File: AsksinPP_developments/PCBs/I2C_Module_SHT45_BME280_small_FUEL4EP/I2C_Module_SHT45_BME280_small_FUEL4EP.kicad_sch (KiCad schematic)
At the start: 13 parts, among them J1 Conn_01x04, U1 BME280, U2 SHT45-AD1B-R2

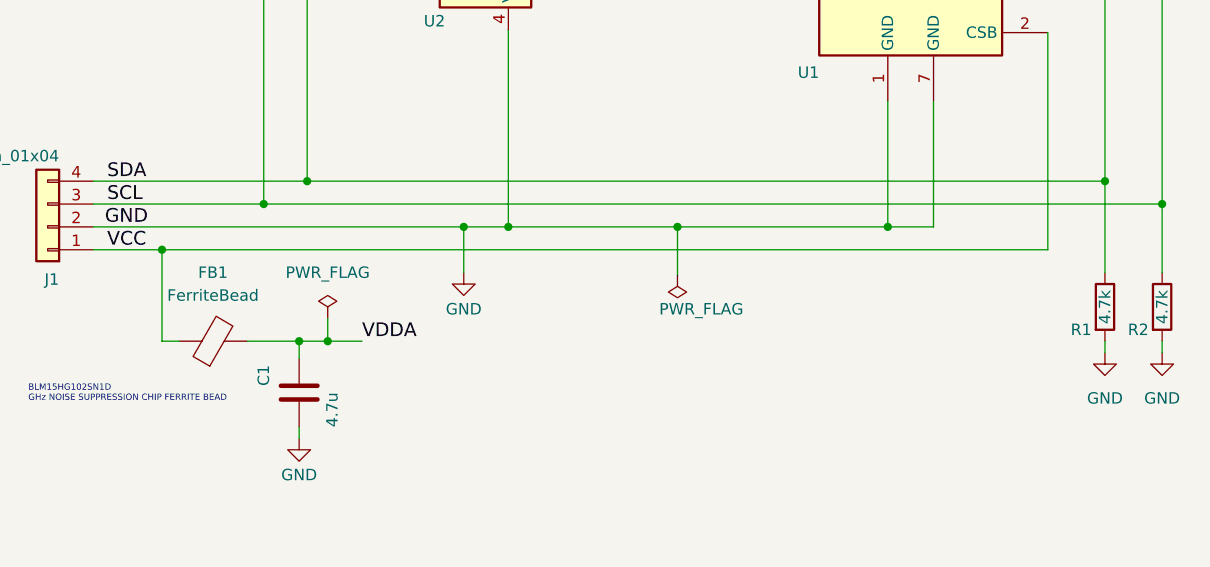
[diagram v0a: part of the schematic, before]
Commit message: PCBs: fix of some project specific KiCAD library paths for portability and missing PWR_FLGs for VCC in some schematics
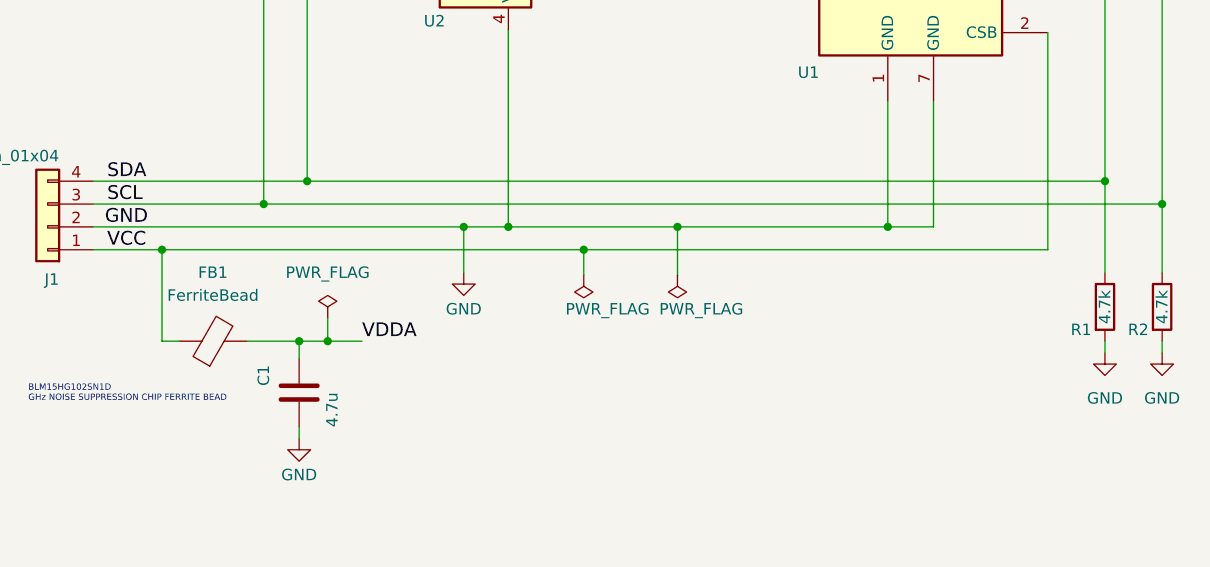
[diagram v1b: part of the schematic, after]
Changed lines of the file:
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@@
   (title_block
     (title "I2C_Module_SHT45_BME280_small_FUEL4EP")
-    (date "2024-01-13")
-    (rev "1.0")
+    (date "2024-01-14")
+    (rev "1.1")
     (company "FUEL4EP")
     (comment 1 "fitting to  HB_Stamp_ATMega1284P_FUEL4EP")
@@
   (junction (at 82.55 124.46) (diameter 0) (color 0 0 0 0)
   )
+  (junction (at 110.998 114.3) (diameter 0) (color 0 0 0 0)
+  )
   (junction (at 102.616 111.76) (diameter 0) (color 0 0 0 0)
   )
@@
     (stroke (width 0) (type default) (color 0 0 0 0))
   )
+  (wire (pts (xy 110.998 114.3) (xy 162.56 114.3))
+    (stroke (width 0) (type default) (color 0 0 0 0))
+  )
   (wire (pts (xy 121.412 111.76) (xy 144.78 111.76))
     (stroke (width 0) (type default) (color 0 0 0 0))
@@
     (stroke (width 0) (type default) (color 0 0 0 0))
   )
+  (wire (pts (xy 110.998 117.094) (xy 110.998 114.3))
+    (stroke (width 0) (type default) (color 0 0 0 0))
+  )
   (wire (pts (xy 79.375 133.985) (xy 79.375 135.255))
     (stroke (width 0) (type default) (color 0 0 0 0))
@@
     (stroke (width 0) (type default) (color 0 0 0 0))
   )
-  (wire (pts (xy 64.135 114.3) (xy 162.56 114.3))
+  (wire (pts (xy 64.135 114.3) (xy 110.998 114.3))
     (stroke (width 0) (type default) (color 0 0 0 0))
   )
@@
     (pin "8")
   )
+  (symbol (lib_id "power:PWR_FLAG") (at 110.998 117.094 180) (unit 1)
+    (in_bom yes) (on_board yes)
+    (property "Reference" "#FLG0102" (id 0) (at 110.998 118.999 0)
+      (effects (font (size 1.27 1.27)) hide)
+    )
+    (property "Value" "PWR_FLAG" (id 1) (at 108.966 120.904 0)
+      (effects (font (size 1.27 1.27)) (justify right))
+    )
+    (property "Footprint" "" (id 2) (at 110.998 117.094 0)
+      (effects (font (size 1.27 1.27)) hide)
+    )
+    (property "Datasheet" "~" (id 3) (at 110.998 117.094 0)
+      (effects (font (size 1.27 1.27)) hide)
+    )
+    (pin "1")
+  )
   (symbol (lib_id "Device:C") (at 79.375 130.175 0) (unit 1)
     (in_bom yes) (on_board yes)
@@
       (reference "#FLG0101") (unit 1) (value "PWR_FLAG") (footprint "")
     )
+    (path "/7820c09a-77a5-4506-a798-0f22336e0c44"
+      (reference "#FLG0102") (unit 1) (value "PWR_FLAG") (footprint "")
+    )
     (path "/2fb280af-9352-43f7-93d8-89326fb5dc6f"

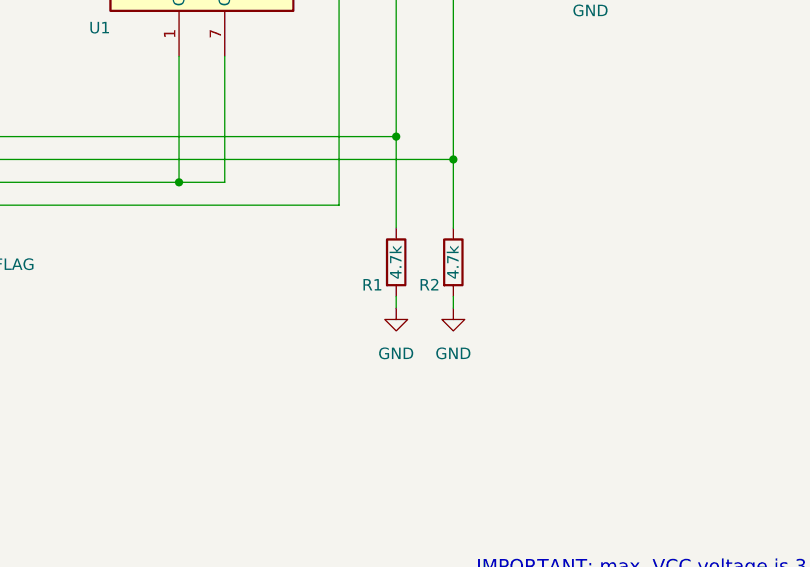
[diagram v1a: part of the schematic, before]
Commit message: PCBs: fix of I2C Pull-up resistors that were wrongly tied to GND
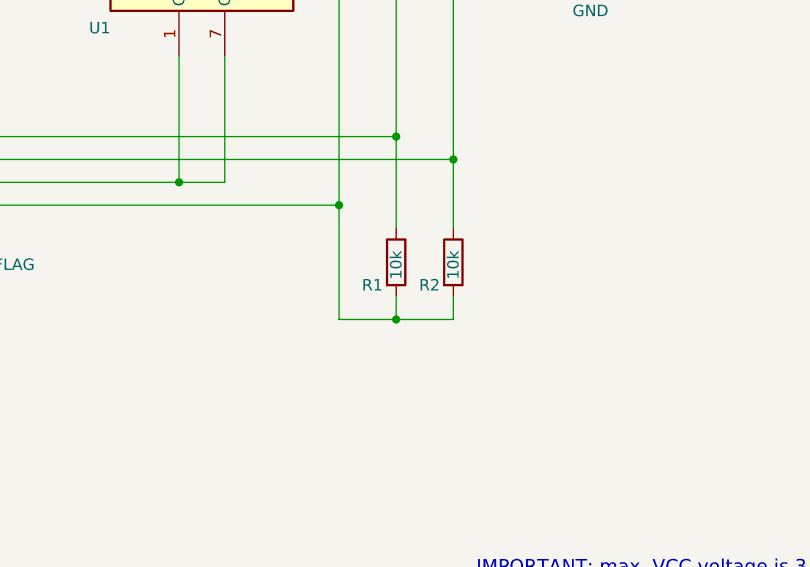
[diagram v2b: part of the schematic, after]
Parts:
- R1, R2: value 4.7k -> 10k; LCSC C25900 -> C25744
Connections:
- net GND: no longer R1.2, R2.2
- net VCC: now also R1.2, R2.2
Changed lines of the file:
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@@
   (title_block
     (title "I2C_Module_SHT45_BME280_small_FUEL4EP")
-    (date "2024-01-14")
-    (rev "1.1")
+    (date "2024-02-08")
+    (rev "1.2")
     (company "FUEL4EP")
     (comment 1 "fitting to  HB_Stamp_ATMega1284P_FUEL4EP")
@@
   (junction (at 64.135 114.3) (diameter 0) (color 0 0 0 0)
   )
+  (junction (at 162.56 114.3) (diameter 0) (color 0 0 0 0)
+  )
   (junction (at 154.94 58.42) (diameter 0) (color 0 0 0 0)
   )
+  (junction (at 168.91 127) (diameter 0) (color 0 0 0 0)
+  )
   (junction (at 79.375 124.46) (diameter 0) (color 0 0 0 0)
   )
@@
     (stroke (width 0) (type default) (color 0 0 0 0))
   )
+  (wire (pts (xy 162.56 127) (xy 162.56 114.3))
+    (stroke (width 0) (type default) (color 0 0 0 0))
+  )
   (wire (pts (xy 80.264 106.68) (xy 168.91 106.68))
     (stroke (width 0) (type default) (color 0 0 0 0))
@@
     (stroke (width 0) (type default) (color 0 0 0 0))
   )
-  (wire (pts (xy 168.91 124.46) (xy 168.91 125.73))
-    (stroke (width 0) (type default) (color 0 0 0 0))
-  )
   (wire (pts (xy 56.515 106.68) (xy 80.264 106.68))
     (stroke (width 0) (type default) (color 0 0 0 0))
@@
     (stroke (width 0) (type default) (color 0 0 0 0))
   )
-  (wire (pts (xy 175.26 124.46) (xy 175.26 125.73))
-    (stroke (width 0) (type default) (color 0 0 0 0))
-  )
   (wire (pts (xy 149.86 58.42) (xy 154.94 58.42))
     (stroke (width 0) (type default) (color 0 0 0 0))
@@
     (stroke (width 0) (type default) (color 0 0 0 0))
   )
+  (wire (pts (xy 168.91 127) (xy 162.56 127))
+    (stroke (width 0) (type default) (color 0 0 0 0))
+  )
+  (wire (pts (xy 175.26 124.46) (xy 175.26 127))
+    (stroke (width 0) (type default) (color 0 0 0 0))
+  )
   (wire (pts (xy 138.43 58.42) (xy 144.78 58.42))
     (stroke (width 0) (type default) (color 0 0 0 0))
@@
     (stroke (width 0) (type default) (color 0 0 0 0))
   )
+  (wire (pts (xy 175.26 127) (xy 168.91 127))
+    (stroke (width 0) (type default) (color 0 0 0 0))
+  )
   (wire (pts (xy 73.66 124.46) (xy 79.375 124.46))
     (stroke (width 0) (type default) (color 0 0 0 0))
@@
   )
   (wire (pts (xy 144.78 97.79) (xy 144.78 111.76))
+    (stroke (width 0) (type default) (color 0 0 0 0))
+  )
+  (wire (pts (xy 168.91 124.46) (xy 168.91 127))
     (stroke (width 0) (type default) (color 0 0 0 0))
   )
@@
       (effects (font (size 1.27 1.27)) (justify left))
     )
-    (property "Value" "4.7k" (id 1) (at 168.91 122.555 90)
+    (property "Value" "10k" (id 1) (at 168.91 122.555 90)
       (effects (font (size 1.27 1.27)) (justify left))
     )
@@
       (effects (font (size 1.27 1.27)) hide)
     )
-    (property "LCSC" "C25900" (id 4) (at 168.91 120.65 0)
+    (property "LCSC" "C25744" (id 4) (at 168.91 120.65 0)
       (effects (font (size 1.524 1.524)) hide)
     )
@@
     )
     (property "Datasheet" "" (id 3) (at 93.472 48.768 0)
-      (effects (font (size 1.27 1.27)) hide)
-    )
-    (pin "1")
-  )
-  (symbol (lib_id "power:GND") (at 168.91 125.73 0) (unit 1)
-    (in_bom yes) (on_board yes) (fields_autoplaced)
-    (property "Reference" "#PWR07" (id 0) (at 168.91 132.08 0)
-      (effects (font (size 1.27 1.27)) hide)
-    )
-    (property "Value" "GND" (id 1) (at 168.91 130.81 0))
-    (property "Footprint" "" (id 2) (at 168.91 125.73 0)
-      (effects (font (size 1.27 1.27)) hide)
-    )
-    (property "Datasheet" "" (id 3) (at 168.91 125.73 0)
       (effects (font (size 1.27 1.27)) hide)
     )
@@
     (pin "1")
   )
-  (symbol (lib_id "power:GND") (at 175.26 125.73 0) (unit 1)
-    (in_bom yes) (on_board yes) (fields_autoplaced)
-    (property "Reference" "#PWR08" (id 0) (at 175.26 132.08 0)
-      (effects (font (size 1.27 1.27)) hide)
-    )
-    (property "Value" "GND" (id 1) (at 175.26 130.81 0))
-    (property "Footprint" "" (id 2) (at 175.26 125.73 0)
-      (effects (font (size 1.27 1.27)) hide)
-    )
-    (property "Datasheet" "" (id 3) (at 175.26 125.73 0)
-      (effects (font (size 1.27 1.27)) hide)
-    )
-    (pin "1")
-  )
   (symbol (lib_id "power:VDDA") (at 167.64 48.26 0) (unit 1)
     (in_bom yes) (on_board yes) (fields_autoplaced)
@@
       (effects (font (size 1.27 1.27)) (justify left))
     )
-    (property "Value" "4.7k" (id 1) (at 175.26 122.555 90)
+    (property "Value" "10k" (id 1) (at 175.26 122.555 90)
       (effects (font (size 1.27 1.27)) (justify left))
     )
@@
       (effects (font (size 1.27 1.27)) hide)
     )
-    (property "LCSC" "C25900" (id 4) (at 175.26 120.65 0)
+    (property "LCSC" "C25744" (id 4) (at 175.26 120.65 0)
       (effects (font (size 1.524 1.524)) hide)
     )
@@
       (reference "#PWR06") (unit 1) (value "VDDA") (footprint "")
     )
-    (path "/18542ab6-239f-4332-a70c-3c8551b285bb"
-      (reference "#PWR07") (unit 1) (value "GND") (footprint "")
-    )
-    (path "/d43541cc-8fb7-4c57-a7c8-5b5588c55acf"
-      (reference "#PWR08") (unit 1) (value "GND") (footprint "")
-    )
     (path "/b9ee5250-0210-4fd4-abf8-6419214a066d"
       (reference "#PWR09") (unit 1) (value "GND") (footprint "")
@@
     )
     (path "/010452d5-e5f2-447e-a153-71da0dbec114"
-      (reference "R1") (unit 1) (value "4.7k") (footprint "Resistor_SMD:R_0402_1005Metric")
+      (reference "R1") (unit 1) (value "10k") (footprint "Resistor_SMD:R_0402_1005Metric")
     )
     (path "/f75dc7be-70bf-4119-8c06-195e1a960dd2"
-      (reference "R2") (unit 1) (value "4.7k") (footprint "Resistor_SMD:R_0402_1005Metric")
+      (reference "R2") (unit 1) (value "10k") (footprint "Resistor_SMD:R_0402_1005Metric")
     )
     (path "/55b96afd-ec19-4400-9134-cc56302d872a"

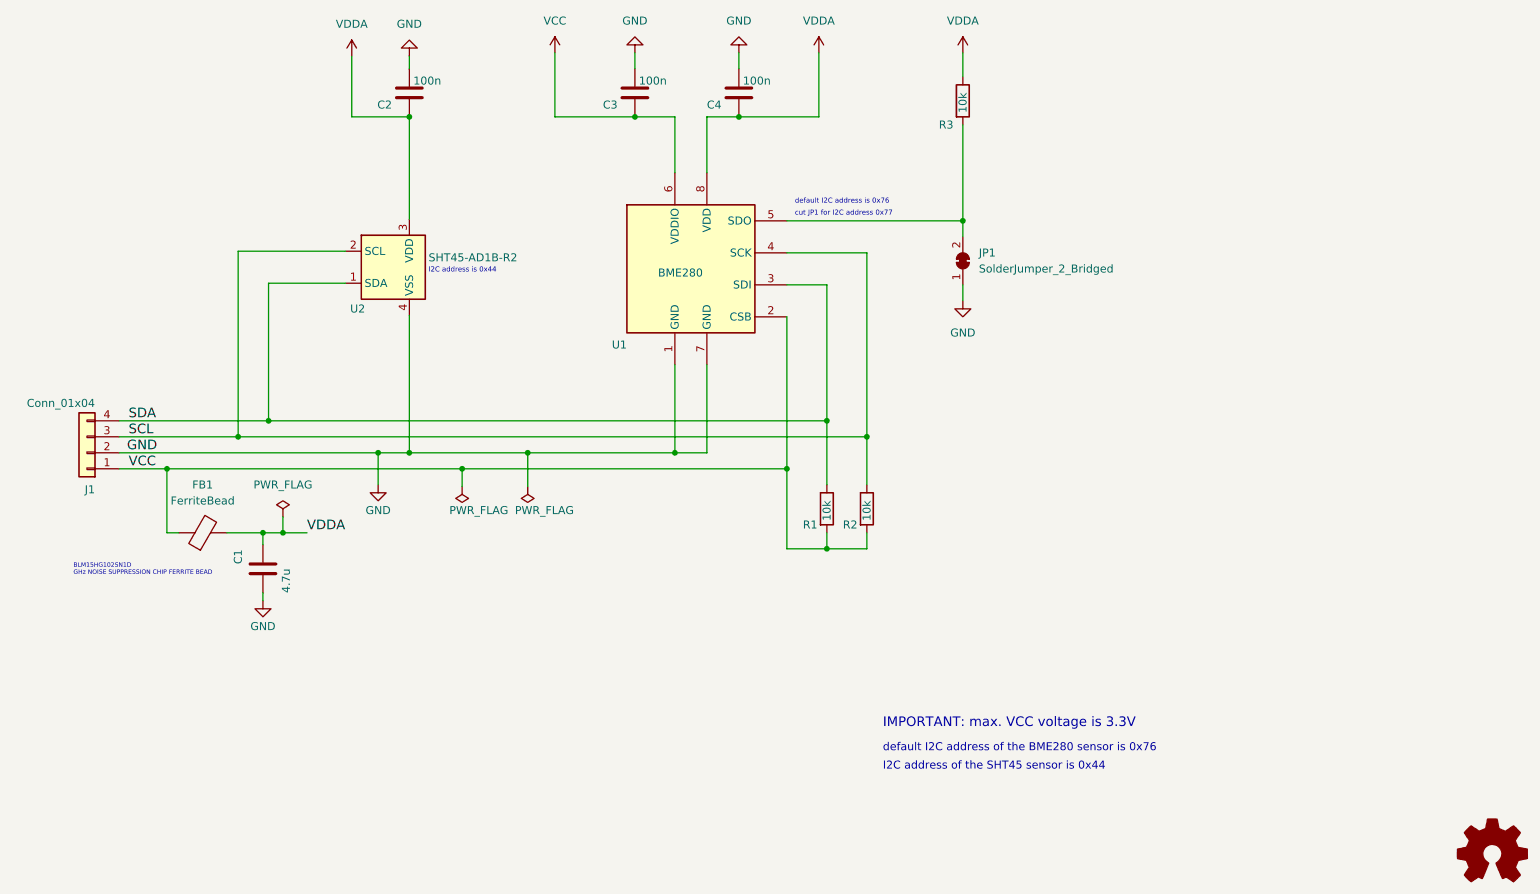
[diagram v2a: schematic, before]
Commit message: PCBs: upgrade some PCBs to KiCAD 7; fix of unnecessary leakage current of I2C address selector: I2C_Module_SHT85_BME280_FUEL4EP, I2C_Module_SHT45_BME280_small_FUEL4EP, I2C_Module_SHT45_BME280_FUEL4EP, I2C_Module_BME280_FUEL4EP, and I2C_Module_BME680_FUEL4EP
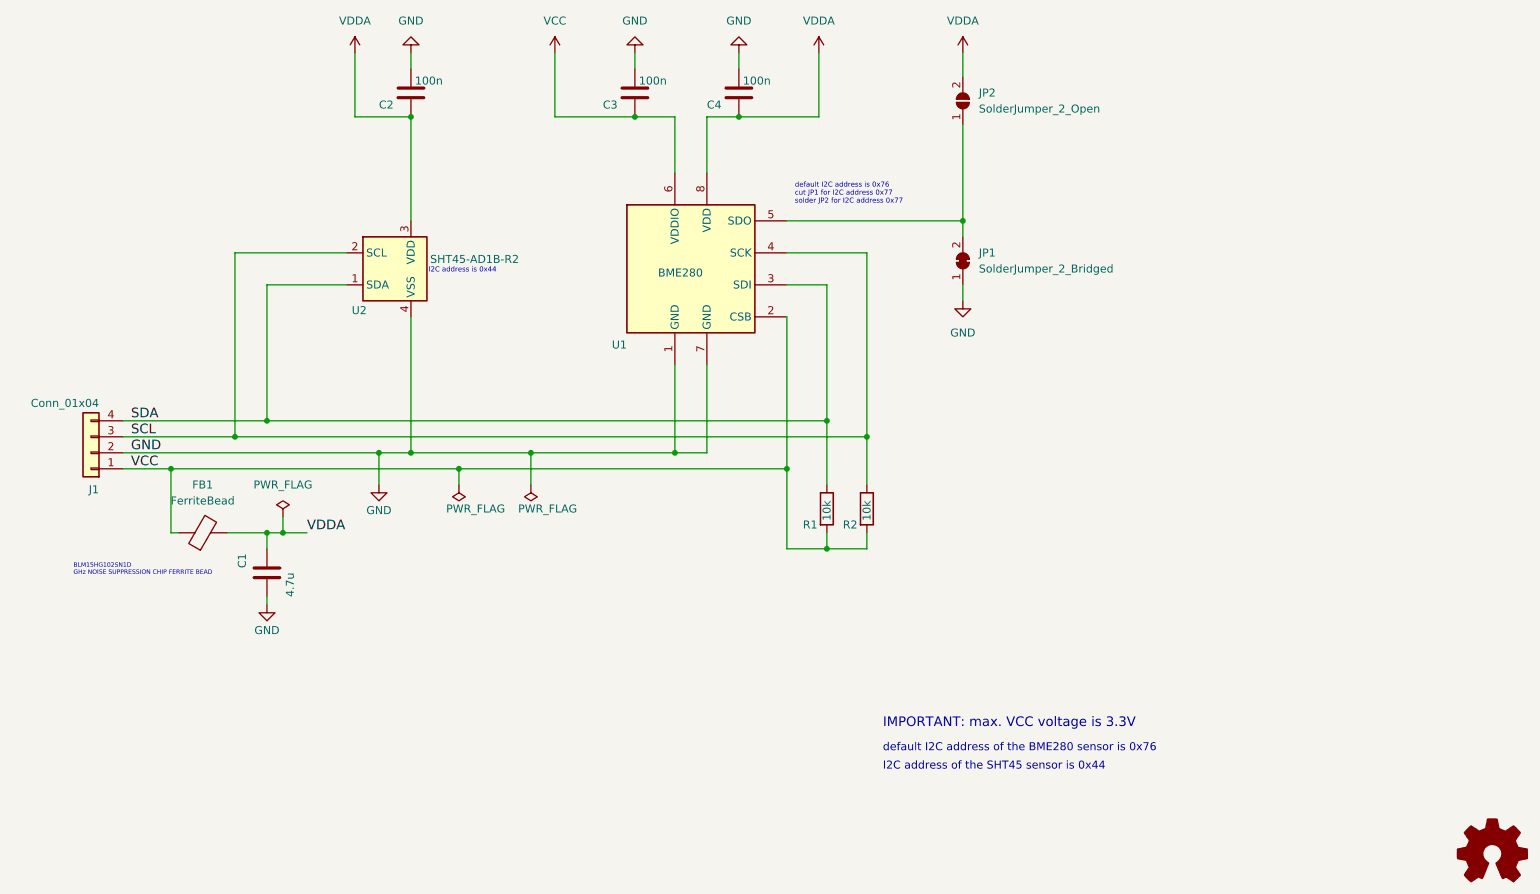
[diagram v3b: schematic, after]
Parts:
- removed R3: 10k, Resistor_SMD:R_0402_1005Metric, symbol Device:R
- added JP2: SolderJumper_2_Open, Jumper:SolderJumper-2_P1.3mm_Open_Pad1.0x1.5mm, symbol Jumper:SolderJumper_2_Open
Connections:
- net VDDA: now also JP2.2 (B)
- net at JP1.2 (B), U1.5 (SDO): now also JP2.1 (A)
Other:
- note added: "solder JP2 for I2C address 0x77"
- moved on the sheet: C1, J1

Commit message: PCBs/I2C_Module_SHT45_BME280_small_FUEL4EP: migration to KiCAD 8
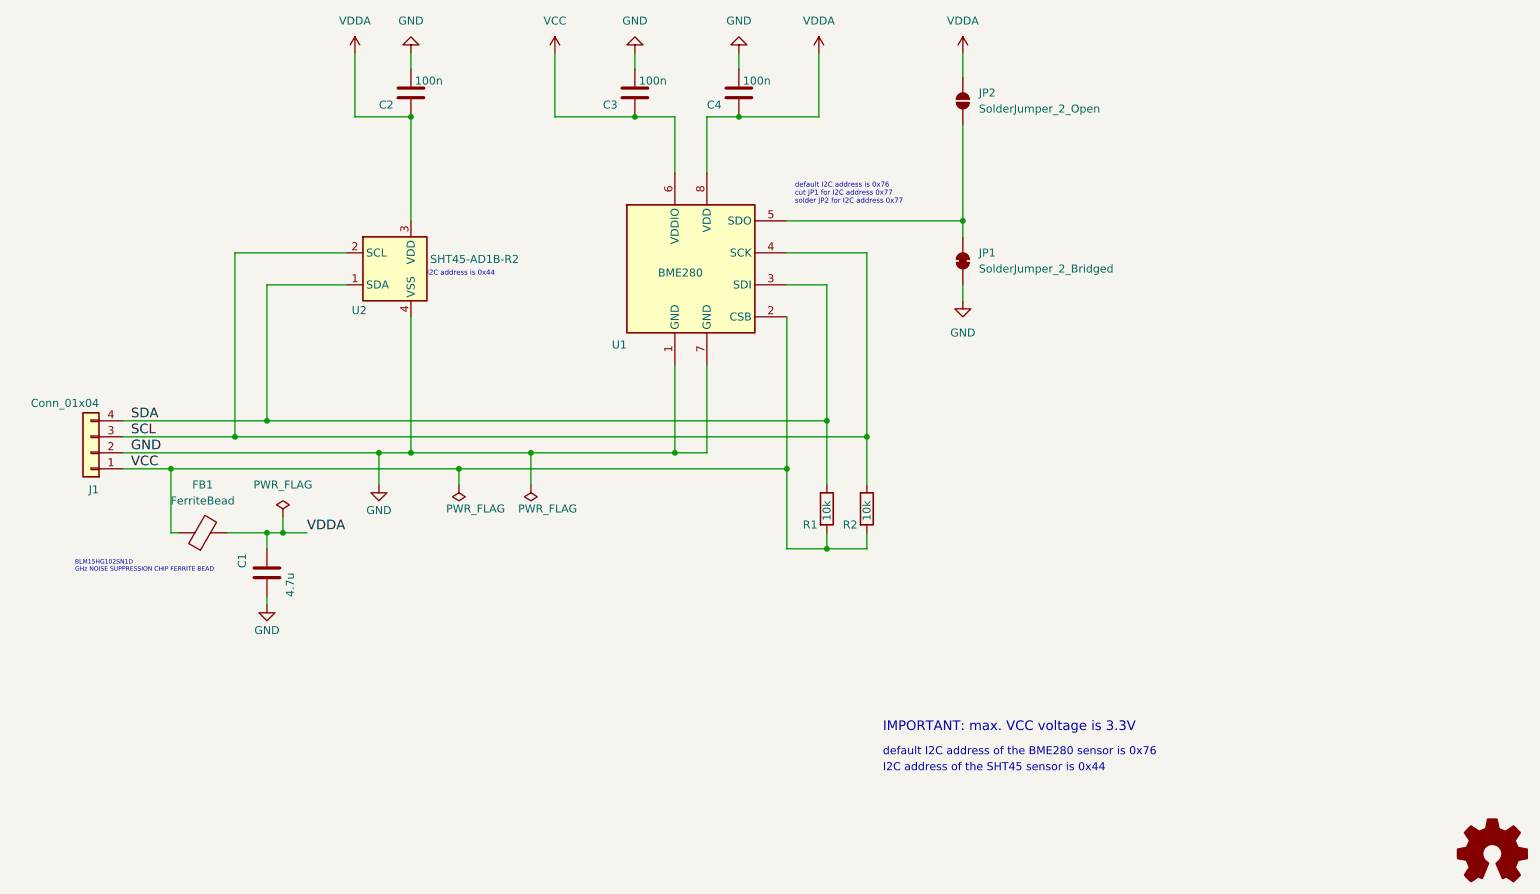
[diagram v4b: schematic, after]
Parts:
- U2: footprint FUEL4EP:SHT4X -> Sensor_Humidity:Sensirion_DFN-4_1.5x1.5mm_P0.8mm_SHT4x_NoCentralPad
